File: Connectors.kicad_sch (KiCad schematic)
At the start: 4 parts

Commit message: Annotation
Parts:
- gave numbers to parts that had none: 4
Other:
- moved on the sheet: J1, J2, J3, J4
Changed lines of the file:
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@@
     (company "GM Industries")
   )
-  (symbol (lib_id "Connector_Generic:Conn_01x09") (at 91.44 59.69 0) (unit 1)
+  (symbol (lib_id "Connector_Generic:Conn_01x09") (at 101.6 99.06 0) (unit 1)
     (in_bom yes) (on_board yes) (fields_autoplaced)
-    (property "Reference" "J?" (id 0) (at 93.98 58.4199 0)
+    (property "Reference" "J2" (id 0) (at 104.14 97.7899 0)
       (effects (font (size 1.27 1.27)) (justify left))
     )
-    (property "Value" "Conn_01x09" (id 1) (at 93.98 60.9599 0)
+    (property "Value" "Conn_01x09" (id 1) (at 104.14 100.3299 0)
       (effects (font (size 1.27 1.27)) (justify left))
     )
-    (property "Footprint" "" (id 2) (at 91.44 59.69 0)
+    (property "Footprint" "" (id 2) (at 101.6 99.06 0)
       (effects (font (size 1.27 1.27)) hide)
     )
-    (property "Datasheet" "~" (id 3) (at 91.44 59.69 0)
+    (property "Datasheet" "~" (id 3) (at 101.6 99.06 0)
       (effects (font (size 1.27 1.27)) hide)
     )
@@
     (pin "9")
   )
-  (symbol (lib_id "Connector_Generic:Conn_02x03_Odd_Even") (at 144.78 74.93 0) (unit 1)
+  (symbol (lib_id "Connector_Generic:Conn_02x03_Odd_Even") (at 142.24 99.06 0) (unit 1)
     (in_bom yes) (on_board yes) (fields_autoplaced)
-    (property "Reference" "J?" (id 0) (at 146.05 66.04 0))
-    (property "Value" "Conn_02x03_Odd_Even" (id 1) (at 146.05 68.58 0))
-    (property "Footprint" "" (id 2) (at 144.78 74.93 0)
+    (property "Reference" "J3" (id 0) (at 143.51 90.17 0))
+    (property "Value" "Conn_02x03_Odd_Even" (id 1) (at 143.51 92.71 0))
+    (property "Footprint" "" (id 2) (at 142.24 99.06 0)
       (effects (font (size 1.27 1.27)) hide)
     )
-    (property "Datasheet" "~" (id 3) (at 144.78 74.93 0)
+    (property "Datasheet" "~" (id 3) (at 142.24 99.06 0)
       (effects (font (size 1.27 1.27)) hide)
     )
@@
     (pin "6")
   )
-  (symbol (lib_id "Connector_Generic:Conn_01x04") (at 144.78 76.2 0) (unit 1)
+  (symbol (lib_id "Connector_Generic:Conn_01x04") (at 144.78 58.42 0) (unit 1)
     (in_bom yes) (on_board yes) (fields_autoplaced)
-    (property "Reference" "J?" (id 0) (at 147.32 76.1999 0)
+    (property "Reference" "J4" (id 0) (at 147.32 58.4199 0)
       (effects (font (size 1.27 1.27)) (justify left))
     )
-    (property "Value" "Conn_01x04" (id 1) (at 147.32 78.7399 0)
+    (property "Value" "Conn_01x04" (id 1) (at 147.32 60.9599 0)
       (effects (font (size 1.27 1.27)) (justify left))
     )
-    (property "Footprint" "" (id 2) (at 144.78 76.2 0)
+    (property "Footprint" "" (id 2) (at 144.78 58.42 0)
       (effects (font (size 1.27 1.27)) hide)
     )
-    (property "Datasheet" "~" (id 3) (at 144.78 76.2 0)
+    (property "Datasheet" "~" (id 3) (at 144.78 58.42 0)
       (effects (font (size 1.27 1.27)) hide)
     )
@@
     (pin "4")
   )
-  (symbol (lib_id "Connector_Generic:Conn_01x04") (at 146.05 55.88 0) (unit 1)
+  (symbol (lib_id "Connector_Generic:Conn_01x04") (at 99.06 58.42 0) (unit 1)
     (in_bom yes) (on_board yes) (fields_autoplaced)
-    (property "Reference" "J?" (id 0) (at 148.59 55.8799 0)
+    (property "Reference" "J1" (id 0) (at 101.6 58.4199 0)
       (effects (font (size 1.27 1.27)) (justify left))
     )
-    (property "Value" "Conn_01x04" (id 1) (at 148.59 58.4199 0)
+    (property "Value" "Conn_01x04" (id 1) (at 101.6 60.9599 0)
       (effects (font (size 1.27 1.27)) (justify left))
     )
-    (property "Footprint" "" (id 2) (at 146.05 55.88 0)
+    (property "Footprint" "" (id 2) (at 99.06 58.42 0)
       (effects (font (size 1.27 1.27)) hide)
     )
-    (property "Datasheet" "~" (id 3) (at 146.05 55.88 0)
+    (property "Datasheet" "~" (id 3) (at 99.06 58.42 0)
       (effects (font (size 1.27 1.27)) hide)
     )

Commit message: Component associations and values
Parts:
- J1, J4: value Conn_01x04 -> (none)
- J2: value Conn_01x09 -> (none)
- J3: value Conn_02x03_Odd_Even -> (none)
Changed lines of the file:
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@@
       (effects (font (size 1.27 1.27)) (justify left))
     )
-    (property "Value" "Conn_01x09" (id 1) (at 104.14 100.3299 0)
+    (property "Value" "" (id 1) (at 104.14 100.3299 0)
       (effects (font (size 1.27 1.27)) (justify left))
     )
@@
     (in_bom yes) (on_board yes) (fields_autoplaced)
     (property "Reference" "J3" (id 0) (at 143.51 90.17 0))
-    (property "Value" "Conn_02x03_Odd_Even" (id 1) (at 143.51 92.71 0))
+    (property "Value" "" (id 1) (at 143.51 92.71 0))
     (property "Footprint" "" (id 2) (at 142.24 99.06 0)
       (effects (font (size 1.27 1.27)) hide)
@@
       (effects (font (size 1.27 1.27)) (justify left))
     )
-    (property "Value" "Conn_01x04" (id 1) (at 147.32 60.9599 0)
+    (property "Value" "" (id 1) (at 147.32 60.9599 0)
       (effects (font (size 1.27 1.27)) (justify left))
     )
@@
       (effects (font (size 1.27 1.27)) (justify left))
     )
-    (property "Value" "Conn_01x04" (id 1) (at 101.6 60.9599 0)
+    (property "Value" "" (id 1) (at 101.6 60.9599 0)
       (effects (font (size 1.27 1.27)) (justify left))
     )

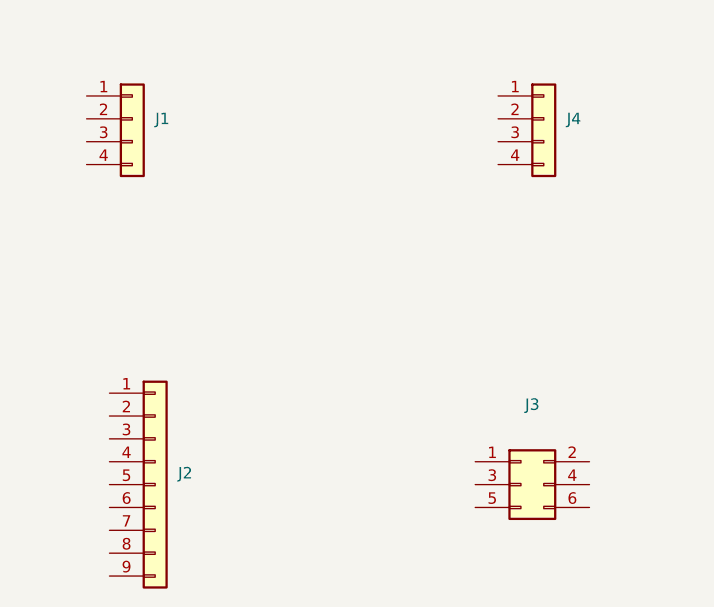
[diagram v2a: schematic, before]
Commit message: Connectors sheet wiring
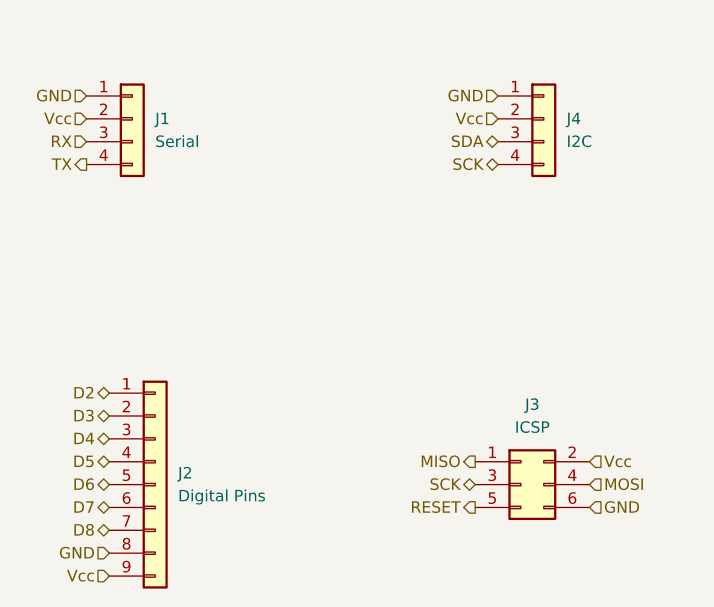
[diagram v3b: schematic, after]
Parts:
- J1: value (none) -> Serial; footprint (none) -> Connector_PinHeader_2.54mm:PinHeader_1x04_P2.54mm_Vertical
- J2: value (none) -> Digital Pins; footprint (none) -> Connector_PinHeader_2.54mm:PinHeader_1x09_P2.54mm_Vertical
- J3: value (none) -> ICSP; footprint (none) -> Connector_PinHeader_2.54mm:PinHeader_2x03_P2.54mm_Vertical
- J4: value (none) -> I2C; footprint (none) -> Connector_PinHeader_2.54mm:PinHeader_1x04_P2.54mm_Vertical
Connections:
- net D2: now reaches J2.1 (Pin_1)
- net D3: now reaches J2.2 (Pin_2)
- net D4: now reaches J2.3 (Pin_3)
- net D5: now reaches J2.4 (Pin_4)
- net D6: now reaches J2.5 (Pin_5)
- net D7: now reaches J2.6 (Pin_6)
- net D8: now reaches J2.7 (Pin_7)
- net GND: now reaches J2.8 (Pin_8)
- net GND: now also J1.1 (Pin_1), J3.6 (Pin_6), J4.1 (Pin_1)
- net Vcc: now reaches J2.9 (Pin_9)
- net Vcc: now also J1.2 (Pin_2), J3.2 (Pin_2), J4.2 (Pin_2)
- net MISO: now reaches J3.1 (Pin_1)
- net SCK: now reaches J3.3 (Pin_3)
- net SCK: now also J4.4 (Pin_4)
- net MOSI: now reaches J3.4 (Pin_4)
- net RESET: now reaches J3.5 (Pin_5)
- net SDA: now reaches J4.3 (Pin_3)
- net RX: now reaches J1.3 (Pin_3)
- net TX: now reaches J1.4 (Pin_4)
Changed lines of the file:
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@@
     (company "GM Industries")
+  )
+  (hierarchical_label "D4" (shape bidirectional) (at 96.52 93.98 180)
+    (effects (font (size 1.27 1.27)) (justify right))
+  )
+  (hierarchical_label "MISO" (shape output) (at 137.16 96.52 180)
+    (effects (font (size 1.27 1.27)) (justify right))
+  )
+  (hierarchical_label "SDA" (shape bidirectional) (at 139.7 60.96 180)
+    (effects (font (size 1.27 1.27)) (justify right))
+  )
+  (hierarchical_label "TX" (shape output) (at 93.98 63.5 180)
+    (effects (font (size 1.27 1.27)) (justify right))
+  )
+  (hierarchical_label "D6" (shape bidirectional) (at 96.52 99.06 180)
+    (effects (font (size 1.27 1.27)) (justify right))
+  )
+  (hierarchical_label "Vcc" (shape input) (at 149.86 96.52 0)
+    (effects (font (size 1.27 1.27)) (justify left))
+  )
+  (hierarchical_label "D5" (shape bidirectional) (at 96.52 96.52 180)
+    (effects (font (size 1.27 1.27)) (justify right))
+  )
+  (hierarchical_label "GND" (shape input) (at 96.52 106.68 180)
+    (effects (font (size 1.27 1.27)) (justify right))
+  )
+  (hierarchical_label "Vcc" (shape input) (at 93.98 58.42 180)
+    (effects (font (size 1.27 1.27)) (justify right))
+  )
+  (hierarchical_label "GND" (shape input) (at 149.86 101.6 0)
+    (effects (font (size 1.27 1.27)) (justify left))
+  )
+  (hierarchical_label "GND" (shape input) (at 93.98 55.88 180)
+    (effects (font (size 1.27 1.27)) (justify right))
+  )
+  (hierarchical_label "Vcc" (shape input) (at 96.52 109.22 180)
+    (effects (font (size 1.27 1.27)) (justify right))
+  )
+  (hierarchical_label "RESET" (shape output) (at 137.16 101.6 180)
+    (effects (font (size 1.27 1.27)) (justify right))
+  )
+  (hierarchical_label "D8" (shape bidirectional) (at 96.52 104.14 180)
+    (effects (font (size 1.27 1.27)) (justify right))
+  )
+  (hierarchical_label "D7" (shape bidirectional) (at 96.52 101.6 180)
+    (effects (font (size 1.27 1.27)) (justify right))
+  )
+  (hierarchical_label "SCK" (shape bidirectional) (at 137.16 99.06 180)
+    (effects (font (size 1.27 1.27)) (justify right))
+  )
+  (hierarchical_label "D3" (shape bidirectional) (at 96.52 91.44 180)
+    (effects (font (size 1.27 1.27)) (justify right))
+  )
+  (hierarchical_label "GND" (shape input) (at 139.7 55.88 180)
+    (effects (font (size 1.27 1.27)) (justify right))
+  )
+  (hierarchical_label "MOSI" (shape input) (at 149.86 99.06 0)
+    (effects (font (size 1.27 1.27)) (justify left))
+  )
+  (hierarchical_label "RX" (shape input) (at 93.98 60.96 180)
+    (effects (font (size 1.27 1.27)) (justify right))
+  )
+  (hierarchical_label "Vcc" (shape input) (at 139.7 58.42 180)
+    (effects (font (size 1.27 1.27)) (justify right))
+  )
+  (hierarchical_label "D2" (shape bidirectional) (at 96.52 88.9 180)
+    (effects (font (size 1.27 1.27)) (justify right))
+  )
+  (hierarchical_label "SCK" (shape bidirectional) (at 139.7 63.5 180)
+    (effects (font (size 1.27 1.27)) (justify right))
   )
   (symbol (lib_id "Connector_Generic:Conn_01x09") (at 101.6 99.06 0) (unit 1)
@@
       (effects (font (size 1.27 1.27)) (justify left))
     )
-    (property "Value" "" (id 1) (at 104.14 100.3299 0)
+    (property "Value" "Digital Pins" (id 1) (at 104.14 100.3299 0)
       (effects (font (size 1.27 1.27)) (justify left))
     )
-    (property "Footprint" "" (id 2) (at 101.6 99.06 0)
+    (property "Footprint" "Connector_PinHeader_2.54mm:PinHeader_1x09_P2.54mm_Vertical" (id 2) (at 101.6 99.06 0)
       (effects (font (size 1.27 1.27)) hide)
     )
@@
     (in_bom yes) (on_board yes) (fields_autoplaced)
     (property "Reference" "J3" (id 0) (at 143.51 90.17 0))
-    (property "Value" "" (id 1) (at 143.51 92.71 0))
-    (property "Footprint" "" (id 2) (at 142.24 99.06 0)
+    (property "Value" "ICSP" (id 1) (at 143.51 92.71 0))
+    (property "Footprint" "Connector_PinHeader_2.54mm:PinHeader_2x03_P2.54mm_Vertical" (id 2) (at 142.24 99.06 0)
       (effects (font (size 1.27 1.27)) hide)
     )
@@
       (effects (font (size 1.27 1.27)) (justify left))
     )
-    (property "Value" "" (id 1) (at 147.32 60.9599 0)
+    (property "Value" "I2C" (id 1) (at 147.32 60.9599 0)
       (effects (font (size 1.27 1.27)) (justify left))
     )
-    (property "Footprint" "" (id 2) (at 144.78 58.42 0)
+    (property "Footprint" "Connector_PinHeader_2.54mm:PinHeader_1x04_P2.54mm_Vertical" (id 2) (at 144.78 58.42 0)
       (effects (font (size 1.27 1.27)) hide)
     )
@@
       (effects (font (size 1.27 1.27)) (justify left))
     )
-    (property "Value" "" (id 1) (at 101.6 60.9599 0)
+    (property "Value" "Serial" (id 1) (at 101.6 60.9599 0)
       (effects (font (size 1.27 1.27)) (justify left))
     )
-    (property "Footprint" "" (id 2) (at 99.06 58.42 0)
+    (property "Footprint" "Connector_PinHeader_2.54mm:PinHeader_1x04_P2.54mm_Vertical" (id 2) (at 99.06 58.42 0)
       (effects (font (size 1.27 1.27)) hide)
     )

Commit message: Root sheet wiring
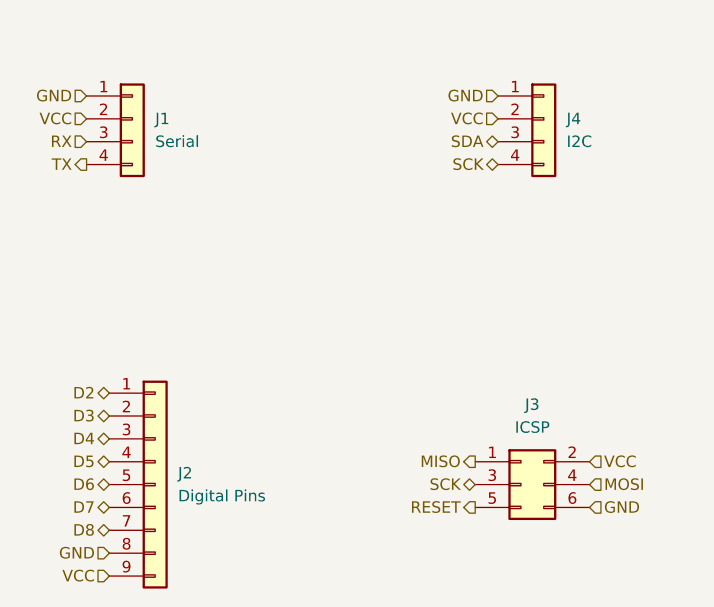
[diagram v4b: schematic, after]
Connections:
- net Vcc renamed VCC
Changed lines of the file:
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@@
     (effects (font (size 1.27 1.27)) (justify right))
   )
-  (hierarchical_label "Vcc" (shape input) (at 149.86 96.52 0)
+  (hierarchical_label "VCC" (shape input) (at 149.86 96.52 0)
     (effects (font (size 1.27 1.27)) (justify left))
   )
@@
     (effects (font (size 1.27 1.27)) (justify right))
   )
-  (hierarchical_label "Vcc" (shape input) (at 93.98 58.42 180)
+  (hierarchical_label "VCC" (shape input) (at 93.98 58.42 180)
     (effects (font (size 1.27 1.27)) (justify right))
   )
@@
     (effects (font (size 1.27 1.27)) (justify right))
   )
-  (hierarchical_label "Vcc" (shape input) (at 96.52 109.22 180)
+  (hierarchical_label "VCC" (shape input) (at 96.52 109.22 180)
     (effects (font (size 1.27 1.27)) (justify right))
   )
@@
     (effects (font (size 1.27 1.27)) (justify right))
   )
-  (hierarchical_label "Vcc" (shape input) (at 139.7 58.42 180)
+  (hierarchical_label "VCC" (shape input) (at 139.7 58.42 180)
     (effects (font (size 1.27 1.27)) (justify right))
   )
